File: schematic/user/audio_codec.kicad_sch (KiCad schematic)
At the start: 31 parts, among them U4 TLV320AIC3254IRHBR

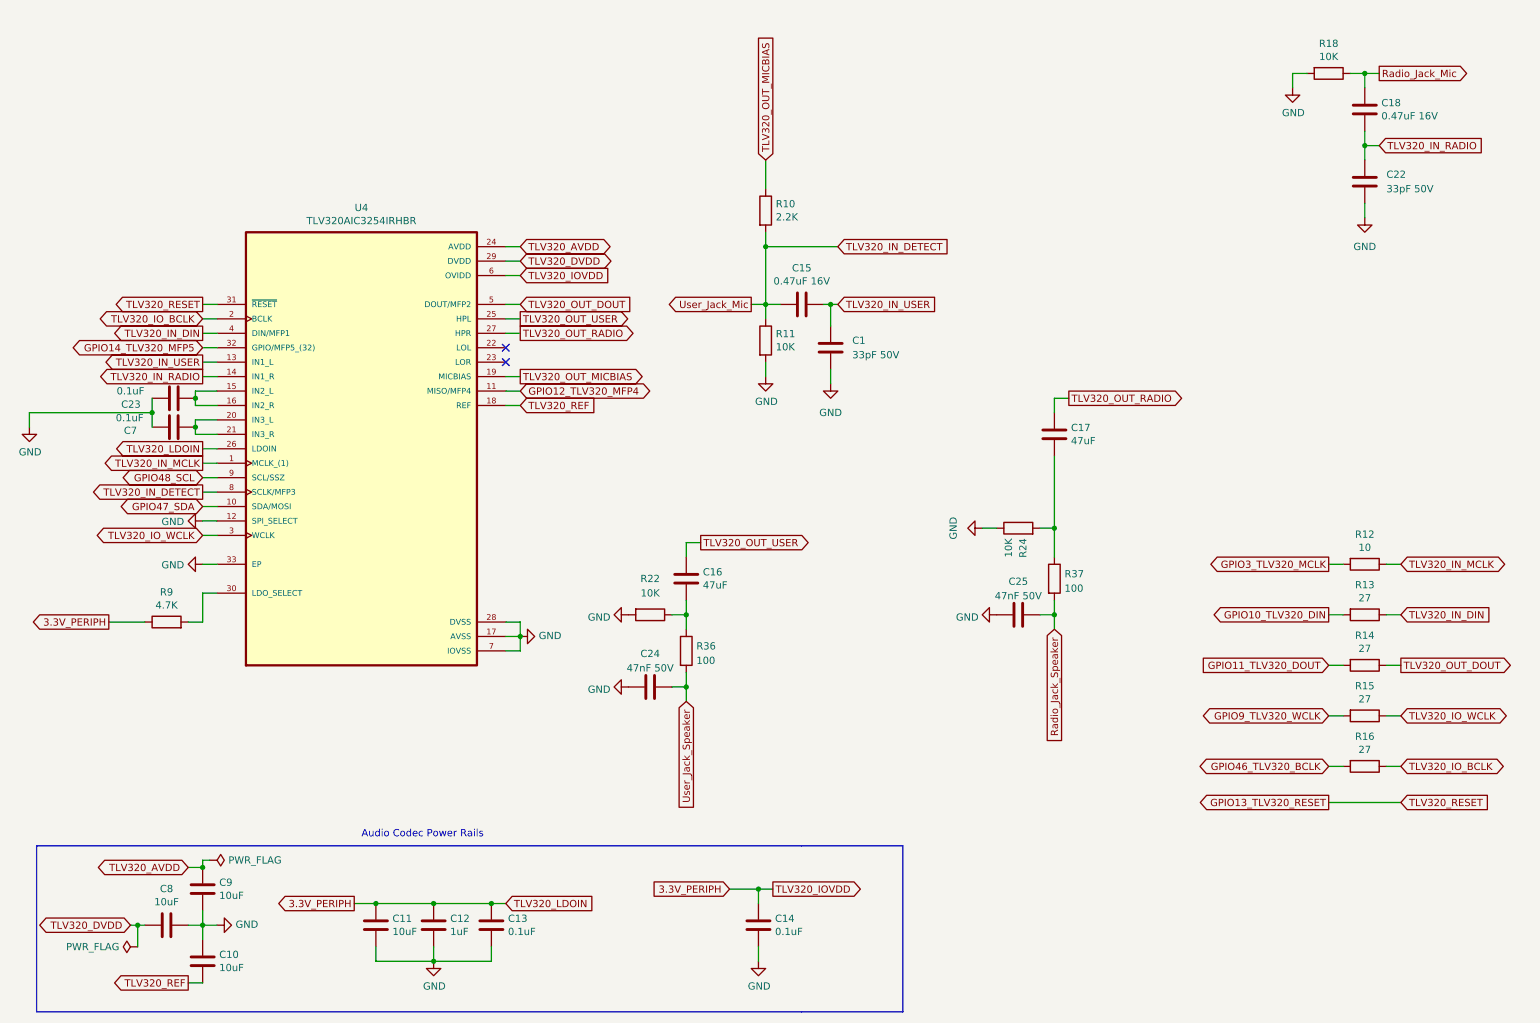
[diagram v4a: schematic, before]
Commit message: v0.7 board: resolve all ERC errors in schematic.
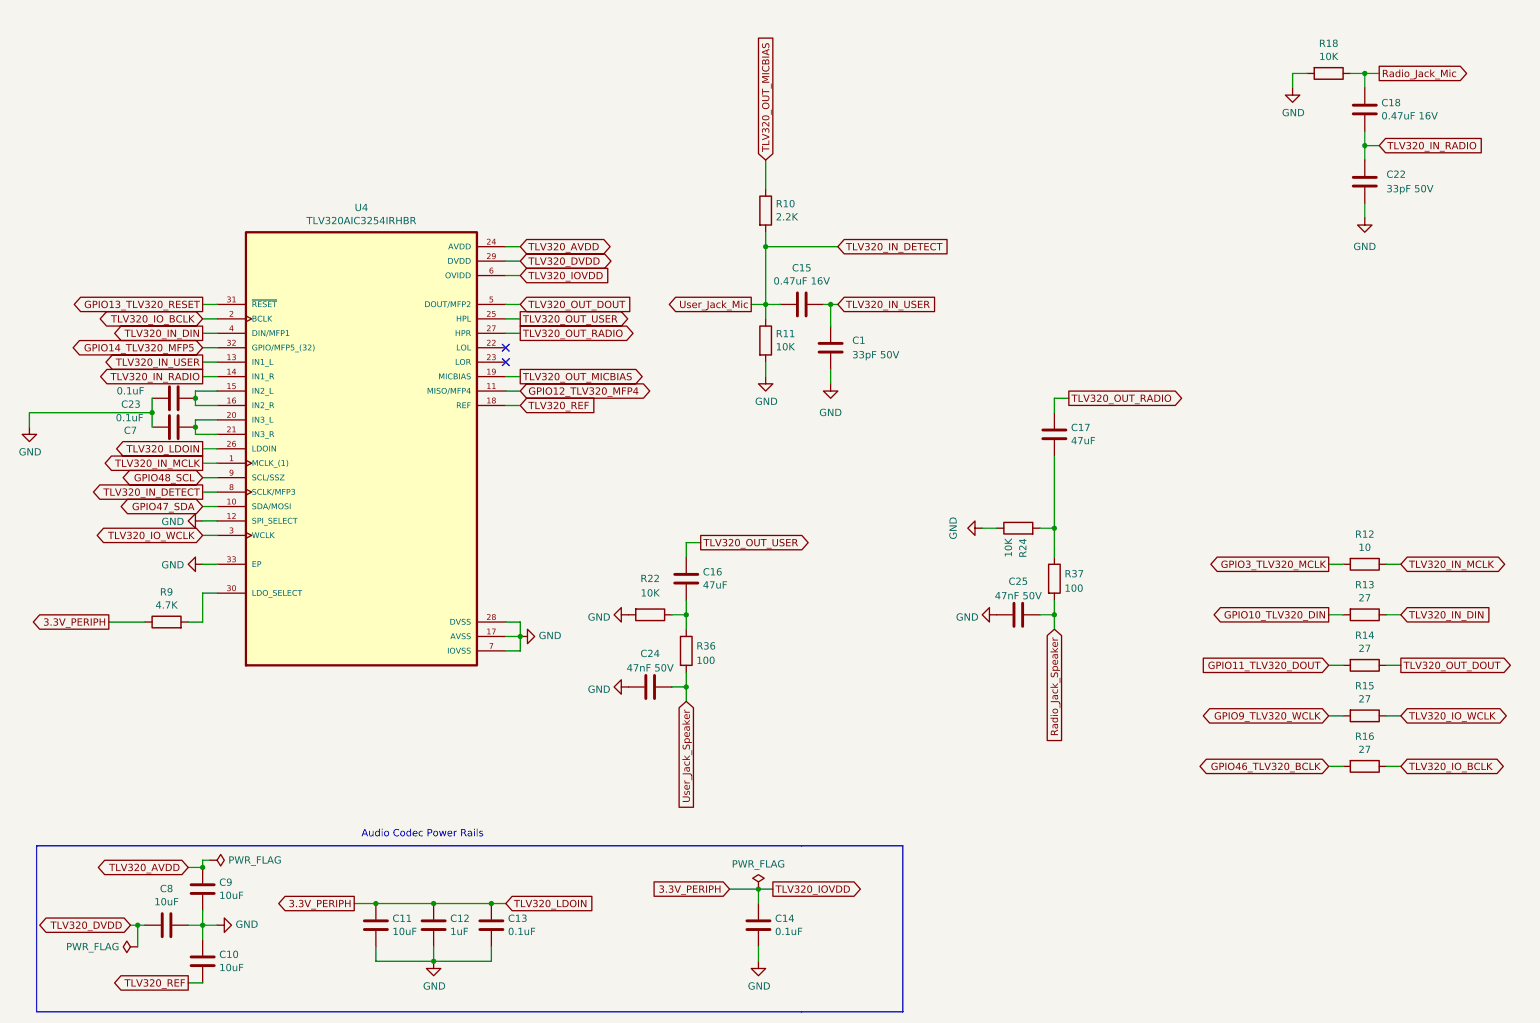
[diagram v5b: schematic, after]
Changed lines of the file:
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@@
-    (stroke (width 0) (type default) (color 0 0 0 0))
-  )
-  (wire (pts (xy 248.92 156.21) (xy 261.62 156.21))
     (stroke (width 0) (type default) (color 0 0 0 0))
   )
@@
     )
   )
-  (global_label "GPIO13_TLV320_RESET" (shape output) (at 248.92 156.21 180) (fields_autoplaced)
-    (effects (font (size 1.27 1.27)) (justify right))
+  (global_label "GPIO13_TLV320_RESET" (shape output) (at 50.8 68.58 180) (fields_autoplaced)
+    (effects (font (size 1.27 1.27)) (justify right))
+    (property "Intersheet References" "${INTERSHEET_REFS}" (id 0) (at -170.18 -55.88 0)
+      (effects (font (size 1.27 1.27)) hide)
+    )
+  )
+  (global_label "TLV320_AVDD" (shape bidirectional) (at 106.68 58.42 0) (fields_autoplaced)
+    (effects (font (size 1.27 1.27)) (justify left))
+    (property "Intersheet References" "${INTERSHEET_REFS}" (id 0) (at -2.54 7.62 0)
+      (effects (font (size 1.27 1.27)) hide)
+    )
+  )
+  (global_label "User_Jack_Mic" (shape output) (at 147.32 68.58 180) (fields_autoplaced)
+    (effects (font (size 1.27 1.27)) (justify right))
+    (property "Intersheet References" "${INTERSHEET_REFS}" (id 0) (at -2.54 7.62 0)
+      (effects (font (size 1.27 1.27)) hide)
+    )
+  )
+  (global_label "TLV320_IO_BCLK" (shape bidirectional) (at 50.8 71.12 180) (fields_autoplaced)
+    (effects (font (size 1.27 1.27)) (justify right))
+    (property "Intersheet References" "${INTERSHEET_REFS}" (id 0) (at -2.54 7.62 0)
+      (effects (font (size 1.27 1.27)) hide)
+    )
+  )
+  (global_label "Radio_Jack_Speaker" (shape input) (at 200.66 125.73 270) (fields_autoplaced)
+    (effects (font (size 1.27 1.27)) (justify right))
+    (property "Intersheet References" "${INTERSHEET_REFS}" (id 0) (at 234.95 -86.36 0)
+      (effects (font (size 1.27 1.27)) hide)
+    )
+  )
+  (global_label "TLV320_IO_BCLK" (shape bidirectional) (at 261.62 149.86 0) (fields_autoplaced)
+    (effects (font (size 1.27 1.27)) (justify left))
     (property "Intersheet References" "${INTERSHEET_REFS}" (id 0) (at 27.94 31.75 0)
       (effects (font (size 1.27 1.27)) hide)
     )
   )
-  (global_label "TLV320_AVDD" (shape bidirectional) (at 106.68 58.42 0) (fields_autoplaced)
-    (effects (font (size 1.27 1.27)) (justify left))
-    (property "Intersheet References" "${INTERSHEET_REFS}" (id 0) (at -2.54 7.62 0)
-      (effects (font (size 1.27 1.27)) hide)
-    )
-  )
-  (global_label "User_Jack_Mic" (shape output) (at 147.32 68.58 180) (fields_autoplaced)
-    (effects (font (size 1.27 1.27)) (justify right))
-    (property "Intersheet References" "${INTERSHEET_REFS}" (id 0) (at -2.54 7.62 0)
-      (effects (font (size 1.27 1.27)) hide)
-    )
-  )
-  (global_label "TLV320_IO_BCLK" (shape bidirectional) (at 50.8 71.12 180) (fields_autoplaced)
-    (effects (font (size 1.27 1.27)) (justify right))
-    (property "Intersheet References" "${INTERSHEET_REFS}" (id 0) (at -2.54 7.62 0)
-      (effects (font (size 1.27 1.27)) hide)
-    )
-  )
-  (global_label "Radio_Jack_Speaker" (shape input) (at 200.66 125.73 270) (fields_autoplaced)
-    (effects (font (size 1.27 1.27)) (justify right))
-    (property "Intersheet References" "${INTERSHEET_REFS}" (id 0) (at 234.95 -86.36 0)
-      (effects (font (size 1.27 1.27)) hide)
-    )
-  )
-  (global_label "TLV320_IO_BCLK" (shape bidirectional) (at 261.62 149.86 0) (fields_autoplaced)
-    (effects (font (size 1.27 1.27)) (justify left))
+  (global_label "TLV320_OUT_USER" (shape output) (at 106.68 71.12 0) (fields_autoplaced)
+    (effects (font (size 1.27 1.27)) (justify left))
+    (property "Intersheet References" "${INTERSHEET_REFS}" (id 0) (at -2.54 7.62 0)
+      (effects (font (size 1.27 1.27)) hide)
+    )
+  )
+  (global_label "TLV320_REF" (shape output) (at 48.26 187.96 180) (fields_autoplaced)
+    (effects (font (size 1.27 1.27)) (justify right))
+    (property "Intersheet References" "${INTERSHEET_REFS}" (id 0) (at -2.54 7.62 0)
+      (effects (font (size 1.27 1.27)) hide)
+    )
+  )
+  (global_label "TLV320_IN_MCLK" (shape output) (at 50.8 96.52 180) (fields_autoplaced)
+    (effects (font (size 1.27 1.27)) (justify right))
+    (property "Intersheet References" "${INTERSHEET_REFS}" (id 0) (at -2.54 7.62 0)
+      (effects (font (size 1.27 1.27)) hide)
+    )
+  )
+  (global_label "TLV320_LDOIN" (shape output) (at 50.8 93.98 180) (fields_autoplaced)
+    (effects (font (size 1.27 1.27)) (justify right))
+    (property "Intersheet References" "${INTERSHEET_REFS}" (id 0) (at -2.54 7.62 0)
+      (effects (font (size 1.27 1.27)) hide)
+    )
+  )
+  (global_label "GPIO9_TLV320_WCLK" (shape bidirectional) (at 248.92 140.97 180) (fields_autoplaced)
+    (effects (font (size 1.27 1.27)) (justify right))
     (property "Intersheet References" "${INTERSHEET_REFS}" (id 0) (at 27.94 31.75 0)
       (effects (font (size 1.27 1.27)) hide)
     )
   )
-  (global_label "TLV320_OUT_USER" (shape output) (at 106.68 71.12 0) (fields_autoplaced)
-    (effects (font (size 1.27 1.27)) (justify left))
-    (property "Intersheet References" "${INTERSHEET_REFS}" (id 0) (at -2.54 7.62 0)
-      (effects (font (size 1.27 1.27)) hide)
-    )
-  )
-  (global_label "TLV320_RESET" (shape input) (at 261.62 156.21 0) (fields_autoplaced)
-    (effects (font (size 1.27 1.27)) (justify left))
+  (global_label "TLV320_REF" (shape input) (at 106.68 86.36 0) (fields_autoplaced)
+    (effects (font (size 1.27 1.27)) (justify left))
+    (property "Intersheet References" "${INTERSHEET_REFS}" (id 0) (at -2.54 7.62 0)
+      (effects (font (size 1.27 1.27)) hide)
+    )
+  )
+  (global_label "TLV320_IN_DETECT" (shape input) (at 162.56 58.42 0) (fields_autoplaced)
+    (effects (font (size 1.27 1.27)) (justify left))
+    (property "Intersheet References" "${INTERSHEET_REFS}" (id 0) (at -2.54 7.62 0)
+      (effects (font (size 1.27 1.27)) hide)
+    )
+  )
+  (global_label "GPIO46_TLV320_BCLK" (shape bidirectional) (at 248.92 149.86 180) (fields_autoplaced)
+    (effects (font (size 1.27 1.27)) (justify right))
     (property "Intersheet References" "${INTERSHEET_REFS}" (id 0) (at 27.94 31.75 0)
       (effects (font (size 1.27 1.27)) hide)
     )
   )
-  (global_label "TLV320_REF" (shape output) (at 48.26 187.96 180) (fields_autoplaced)
-    (effects (font (size 1.27 1.27)) (justify right))
-    (property "Intersheet References" "${INTERSHEET_REFS}" (id 0) (at -2.54 7.62 0)
-      (effects (font (size 1.27 1.27)) hide)
-    )
-  )
-  (global_label "TLV320_IN_MCLK" (shape output) (at 50.8 96.52 180) (fields_autoplaced)
-    (effects (font (size 1.27 1.27)) (justify right))
-    (property "Intersheet References" "${INTERSHEET_REFS}" (id 0) (at -2.54 7.62 0)
-      (effects (font (size 1.27 1.27)) hide)
-    )
-  )
-  (global_label "TLV320_LDOIN" (shape output) (at 50.8 93.98 180) (fields_autoplaced)
-    (effects (font (size 1.27 1.27)) (justify right))
-    (property "Intersheet References" "${INTERSHEET_REFS}" (id 0) (at -2.54 7.62 0)
-      (effects (font (size 1.27 1.27)) hide)
-    )
-  )
-  (global_label "GPIO9_TLV320_WCLK" (shape bidirectional) (at 248.92 140.97 180) (fields_autoplaced)
-    (effects (font (size 1.27 1.27)) (justify right))
-    (property "Intersheet References" "${INTERSHEET_REFS}" (id 0) (at 27.94 31.75 0)
-      (effects (font (size 1.27 1.27)) hide)
-    )
-  )
-  (global_label "TLV320_REF" (shape input) (at 106.68 86.36 0) (fields_autoplaced)
-    (effects (font (size 1.27 1.27)) (justify left))
-    (property "Intersheet References" "${INTERSHEET_REFS}" (id 0) (at -2.54 7.62 0)
-      (effects (font (size 1.27 1.27)) hide)
-    )
-  )
-  (global_label "TLV320_IN_DETECT" (shape input) (at 162.56 58.42 0) (fields_autoplaced)
-    (effects (font (size 1.27 1.27)) (justify left))
-    (property "Intersheet References" "${INTERSHEET_REFS}" (id 0) (at -2.54 7.62 0)
-      (effects (font (size 1.27 1.27)) hide)
-    )
-  )
-  (global_label "GPIO46_TLV320_BCLK" (shape bidirectional) (at 248.92 149.86 180) (fields_autoplaced)
-    (effects (font (size 1.27 1.27)) (justify right))
-    (property "Intersheet References" "${INTERSHEET_REFS}" (id 0) (at 27.94 31.75 0)
-      (effects (font (size 1.27 1.27)) hide)
-    )
-  )
   (global_label "TLV320_IOVDD" (shape output) (at 151.13 171.45 0) (fields_autoplaced)
     (effects (font (size 1.27 1.27)) (justify left))
     (property "Intersheet References" "${INTERSHEET_REFS}" (id 0) (at 12.7 5.08 0)
-      (effects (font (size 1.27 1.27)) hide)
-    )
-  )
-  (global_label "TLV320_RESET" (shape output) (at 50.8 68.58 180) (fields_autoplaced)
-    (effects (font (size 1.27 1.27)) (justify right))
-    (property "Intersheet References" "${INTERSHEET_REFS}" (id 0) (at -2.54 7.62 0)
       (effects (font (size 1.27 1.27)) hide)
     )
@@
       (effects (font (size 1.27 1.27)) hide)
     )
+    (pin "1")
+  )
+  (symbol (lib_id "power:PWR_FLAG") (at 148.59 171.45 0) (unit 1)
+    (in_bom yes) (on_board yes)
+    (property "Reference" "#FLG0103" (id 0) (at 148.59 169.545 0)
+      (effects (font (size 1.27 1.27)) hide)
+    )
+    (property "Value" "PWR_FLAG" (id 1) (at 148.59 167.0558 0))
+    (property "Footprint" "" (id 2) (at 148.59 171.45 0)
+      (effects (font (size 1.27 1.27)) hide)
+    )
+    (property "Datasheet" "~" (id 3) (at 148.59 171.45 0)
+      (effects (font (size 1.27 1.27)) hide)
+    )
